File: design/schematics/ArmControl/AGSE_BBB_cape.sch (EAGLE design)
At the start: 57 parts, among them Q1 PFET-FQP27P06, Q2 PFET-FQP27P06, Q3 NFET-FQP30N06L, Q4 NFET-FQP30N06L, Q5 PFET-FQP27P06, Q6 PFET-FQP27P06, Q7 NFET-FQP30N06L, Q8 NFET-FQP30N06L, U1 V_REG_LD1085D2

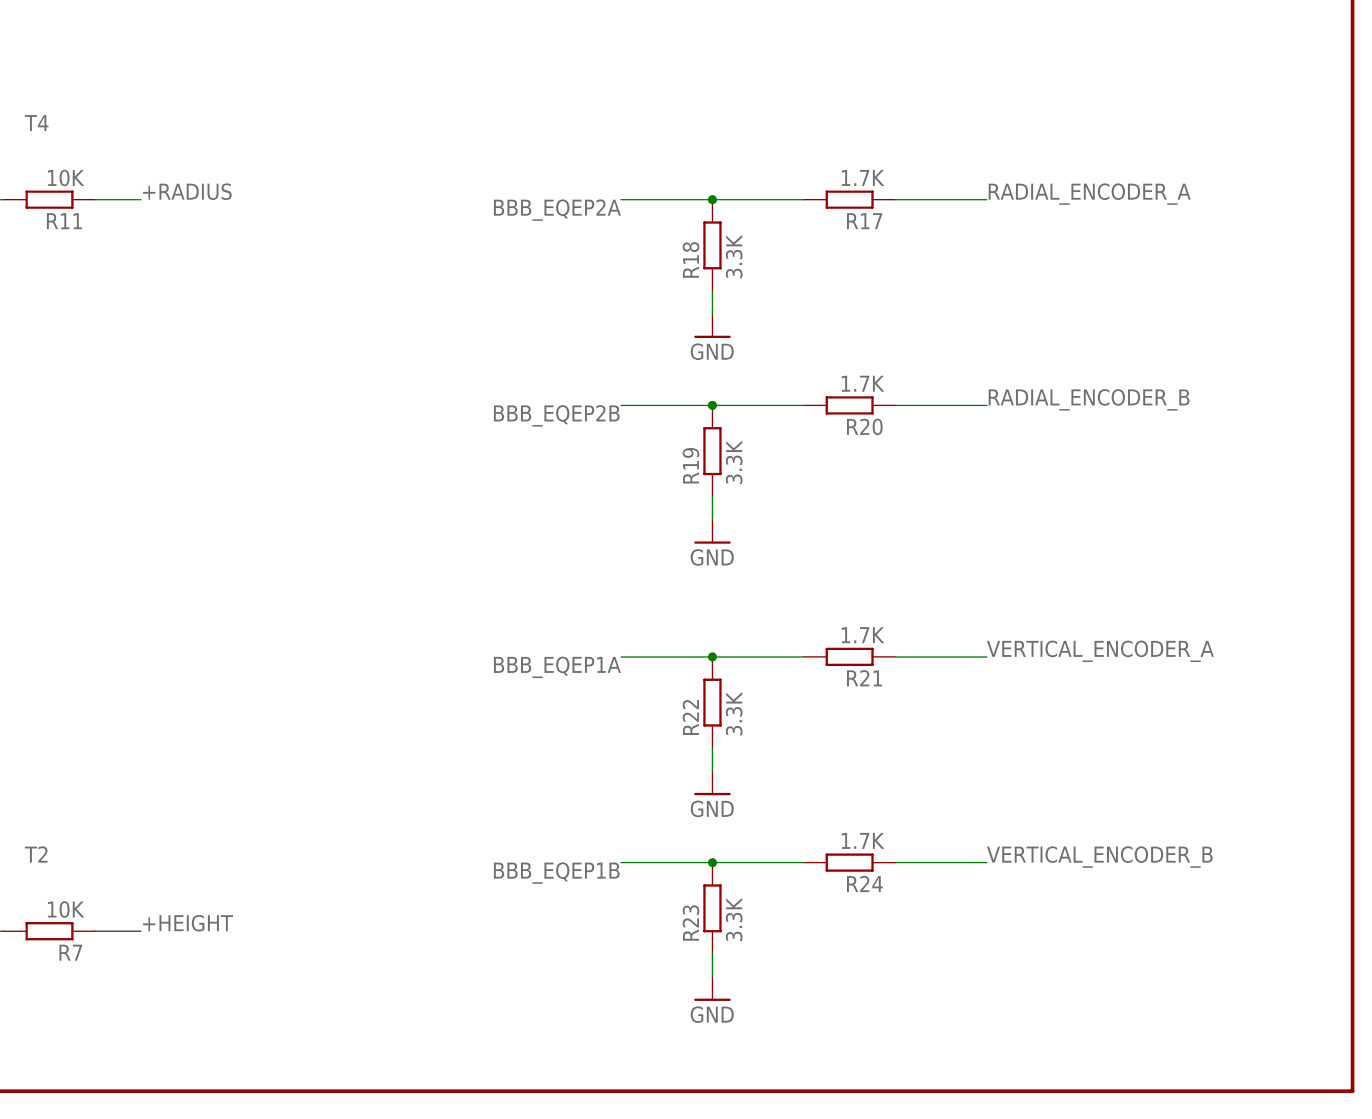
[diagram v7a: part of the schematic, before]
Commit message: Updated board to have molex 4-pin encoder connectors
* also removed unneeded zips
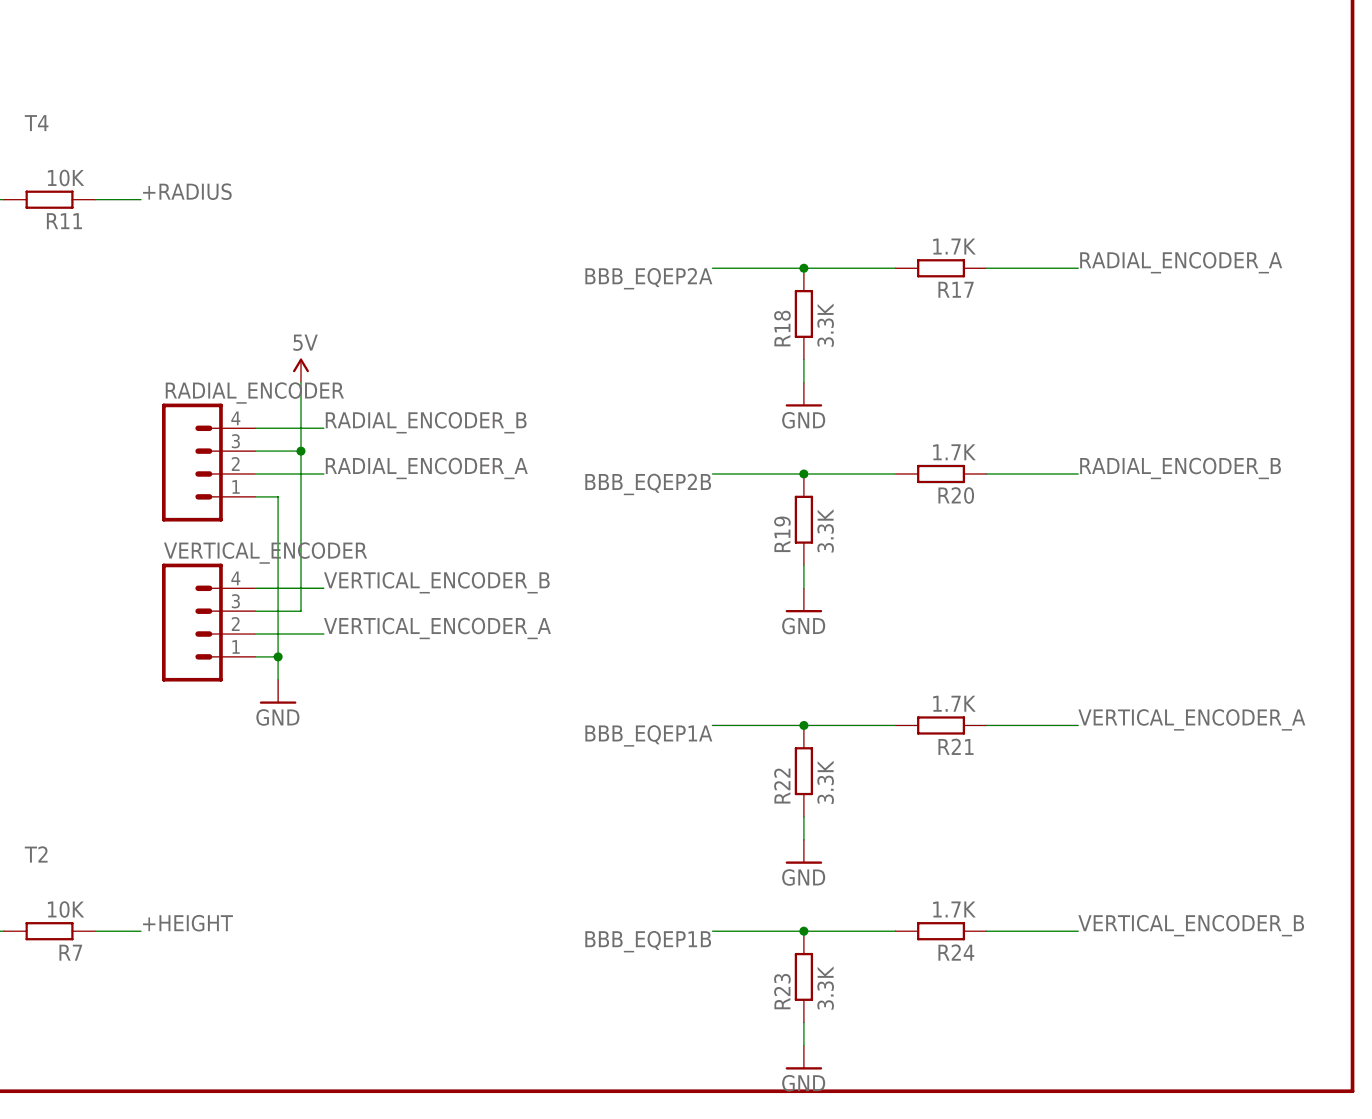
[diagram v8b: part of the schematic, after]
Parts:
- added RADIAL_ENCODER, VERTICAL_ENCODER: (no value), SparkFun-Connectors:M04POLAR
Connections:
- net 5V: now also RADIAL_ENCODER.3, VERTICAL_ENCODER.3
- net GND: now also RADIAL_ENCODER.1, VERTICAL_ENCODER.1
- net RADIAL_ENCODER_A: now also RADIAL_ENCODER.2
- net RADIAL_ENCODER_B: now also RADIAL_ENCODER.4
- net VERTICAL_ENCODER_A: now also VERTICAL_ENCODER.2
- net VERTICAL_ENCODER_B: now also VERTICAL_ENCODER.4
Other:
- moved on the sheet: R17, R18, R19, R20, R21, R22, R23, R24
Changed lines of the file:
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@@
 <part name="R26" library="resistor" deviceset="R-EU_" device="M0805" value="50"/>
 <part name="R27" library="resistor" deviceset="R-EU_" device="M0805" value="50"/>
+<part name="RADIAL_ENCODER" library="SparkFun-Connectors" deviceset="M04" device="POLAR"/>
+<part name="VERTICAL_ENCODER" library="SparkFun-Connectors" deviceset="M04" device="POLAR"/>
+<part name="GND8" library="supply1" deviceset="GND" device=""/>
+<part name="SUPPLY4" library="SparkFun-Aesthetics" deviceset="5V" device=""/>
 </parts>
 <sheets>
@@
 <instance part="R16" gate="G$1" x="208.28" y="121.92" rot="R90"/>
 <instance part="GND12" gate="1" x="208.28" y="111.76"/>
-<instance part="R17" gate="G$1" x="312.42" y="30.48" rot="R180"/>
-<instance part="R18" gate="G$1" x="297.18" y="25.4" rot="R90"/>
-<instance part="R19" gate="G$1" x="297.18" y="2.54" rot="R90"/>
-<instance part="R20" gate="G$1" x="312.42" y="7.62" rot="R180"/>
-<instance part="GND13" gate="1" x="297.18" y="-7.62"/>
-<instance part="GND14" gate="1" x="297.18" y="15.24"/>
-<instance part="R21" gate="G$1" x="312.42" y="-20.32" rot="R180"/>
-<instance part="R22" gate="G$1" x="297.18" y="-25.4" rot="R90"/>
-<instance part="R23" gate="G$1" x="297.18" y="-48.26" rot="R90"/>
-<instance part="R24" gate="G$1" x="312.42" y="-43.18" rot="R180"/>
-<instance part="GND15" gate="1" x="297.18" y="-58.42"/>
-<instance part="GND16" gate="1" x="297.18" y="-35.56"/>
+<instance part="R17" gate="G$1" x="322.58" y="22.86" rot="R180"/>
+<instance part="R18" gate="G$1" x="307.34" y="17.78" rot="R90"/>
+<instance part="R19" gate="G$1" x="307.34" y="-5.08" rot="R90"/>
+<instance part="R20" gate="G$1" x="322.58" y="0" rot="R180"/>
+<instance part="GND13" gate="1" x="307.34" y="-15.24"/>
+<instance part="GND14" gate="1" x="307.34" y="7.62"/>
+<instance part="R21" gate="G$1" x="322.58" y="-27.94" rot="R180"/>
+<instance part="R22" gate="G$1" x="307.34" y="-33.02" rot="R90"/>
+<instance part="R23" gate="G$1" x="307.34" y="-55.88" rot="R90"/>
+<instance part="R24" gate="G$1" x="322.58" y="-50.8" rot="R180"/>
+<instance part="GND15" gate="1" x="307.34" y="-66.04"/>
+<instance part="GND16" gate="1" x="307.34" y="-43.18"/>
 <instance part="FRAME1" gate="G$1" x="-63.5" y="-68.58"/>
 <instance part="FRAME1" gate="G$2" x="-63.5" y="-68.58"/>
@@
 <instance part="R26" gate="G$1" x="91.44" y="-20.32" rot="R90"/>
 <instance part="R27" gate="G$1" x="83.82" y="-20.32" rot="R90"/>
+<instance part="RADIAL_ENCODER" gate="G$1" x="241.3" y="0"/>
+<instance part="VERTICAL_ENCODER" gate="G$1" x="241.3" y="-17.78"/>
+<instance part="GND8" gate="1" x="248.92" y="-25.4"/>
+<instance part="SUPPLY4" gate="G$1" x="251.46" y="10.16"/>
 </instances>
 <busses>
@@
 <pinref part="R19" gate="G$1" pin="1"/>
 <pinref part="GND13" gate="1" pin="GND"/>
-<wire x1="297.18" y1="-5.08" x2="297.18" y2="-2.54" width="0.1524" layer="91"/>
+<wire x1="307.34" y1="-12.7" x2="307.34" y2="-10.16" width="0.1524" layer="91"/>
 </segment>
 <segment>
 <pinref part="R18" gate="G$1" pin="1"/>
 <pinref part="GND14" gate="1" pin="GND"/>
-<wire x1="297.18" y1="17.78" x2="297.18" y2="20.32" width="0.1524" layer="91"/>
+<wire x1="307.34" y1="10.16" x2="307.34" y2="12.7" width="0.1524" layer="91"/>
 </segment>
 <segment>
 <pinref part="R23" gate="G$1" pin="1"/>
 <pinref part="GND15" gate="1" pin="GND"/>
-<wire x1="297.18" y1="-55.88" x2="297.18" y2="-53.34" width="0.1524" layer="91"/>
+<wire x1="307.34" y1="-63.5" x2="307.34" y2="-60.96" width="0.1524" layer="91"/>
 </segment>
 <segment>
 <pinref part="R22" gate="G$1" pin="1"/>
 <pinref part="GND16" gate="1" pin="GND"/>
-<wire x1="297.18" y1="-33.02" x2="297.18" y2="-30.48" width="0.1524" layer="91"/>
+<wire x1="307.34" y1="-40.64" x2="307.34" y2="-38.1" width="0.1524" layer="91"/>
 </segment>
 <segment>
@@
 <junction x="106.68" y="-27.94"/>
 </segment>
+<segment>
+<pinref part="RADIAL_ENCODER" gate="G$1" pin="1"/>
+<wire x1="246.38" y1="-2.54" x2="248.92" y2="-2.54" width="0.1524" layer="91"/>
+<wire x1="248.92" y1="-2.54" x2="248.92" y2="-20.32" width="0.1524" layer="91"/>
+<pinref part="VERTICAL_ENCODER" gate="G$1" pin="1"/>
+<wire x1="248.92" y1="-20.32" x2="248.92" y2="-22.86" width="0.1524" layer="91"/>
+<wire x1="246.38" y1="-20.32" x2="248.92" y2="-20.32" width="0.1524" layer="91"/>
+<junction x="248.92" y="-20.32"/>
+<pinref part="GND8" gate="1" pin="GND"/>
+</segment>
 </net>
 <net name="N$3" class="0">
@@
 <wire x1="345.44" y1="124.46" x2="345.44" y2="132.08" width="0.1524" layer="91"/>
 <pinref part="SUPPLY3" gate="G$1" pin="5V"/>
+</segment>
+<segment>
+<pinref part="VERTICAL_ENCODER" gate="G$1" pin="3"/>
+<wire x1="246.38" y1="-15.24" x2="251.46" y2="-15.24" width="0.1524" layer="91"/>
+<pinref part="SUPPLY4" gate="G$1" pin="5V"/>
+<wire x1="251.46" y1="-15.24" x2="251.46" y2="2.54" width="0.1524" layer="91"/>
+<pinref part="RADIAL_ENCODER" gate="G$1" pin="3"/>
+<wire x1="251.46" y1="2.54" x2="251.46" y2="10.16" width="0.1524" layer="91"/>
+<wire x1="246.38" y1="2.54" x2="251.46" y2="2.54" width="0.1524" layer="91"/>
+<junction x="251.46" y="2.54"/>
 </segment>
 </net>
@@
 <pinref part="R18" gate="G$1" pin="2"/>
 <pinref part="R17" gate="G$1" pin="2"/>
-<wire x1="307.34" y1="30.48" x2="297.18" y2="30.48" width="0.1524" layer="91"/>
-<junction x="297.18" y="30.48"/>
-<wire x1="297.18" y1="30.48" x2="287.02" y2="30.48" width="0.1524" layer="91"/>
-<label x="287.02" y="30.48" size="1.778" layer="95" rot="R180"/>
+<wire x1="317.5" y1="22.86" x2="307.34" y2="22.86" width="0.1524" layer="91"/>
+<junction x="307.34" y="22.86"/>
+<wire x1="307.34" y1="22.86" x2="297.18" y2="22.86" width="0.1524" layer="91"/>
+<label x="297.18" y="22.86" size="1.778" layer="95" rot="R180"/>
 </segment>
 <segment>
@@
 <pinref part="R19" gate="G$1" pin="2"/>
 <pinref part="R20" gate="G$1" pin="2"/>
-<wire x1="307.34" y1="7.62" x2="297.18" y2="7.62" width="0.1524" layer="91"/>
-<junction x="297.18" y="7.62"/>
-<wire x1="297.18" y1="7.62" x2="287.02" y2="7.62" width="0.1524" layer="91"/>
-<label x="287.02" y="7.62" size="1.778" layer="95" rot="R180"/>
+<wire x1="317.5" y1="0" x2="307.34" y2="0" width="0.1524" layer="91"/>
+<junction x="307.34" y="0"/>
+<wire x1="307.34" y1="0" x2="297.18" y2="0" width="0.1524" layer="91"/>
+<label x="297.18" y="0" size="1.778" layer="95" rot="R180"/>
 </segment>
 <segment>
@@
 <segment>
 <pinref part="R20" gate="G$1" pin="1"/>
-<wire x1="317.5" y1="7.62" x2="327.66" y2="7.62" width="0.1524" layer="91"/>
-<label x="327.66" y="7.62" size="1.778" layer="95"/>
+<wire x1="327.66" y1="0" x2="337.82" y2="0" width="0.1524" layer="91"/>
+<label x="337.82" y="0" size="1.778" layer="95"/>
+</segment>
+<segment>
+<pinref part="RADIAL_ENCODER" gate="G$1" pin="4"/>
+<wire x1="246.38" y1="5.08" x2="254" y2="5.08" width="0.1524" layer="91"/>
+<label x="254" y="5.08" size="1.778" layer="95"/>
 </segment>
 </net>
@@
 <segment>
 <pinref part="R17" gate="G$1" pin="1"/>
-<wire x1="317.5" y1="30.48" x2="327.66" y2="30.48" width="0.1524" layer="91"/>
-<label x="327.66" y="30.48" size="1.778" layer="95"/>
+<wire x1="327.66" y1="22.86" x2="337.82" y2="22.86" width="0.1524" layer="91"/>
+<label x="337.82" y="22.86" size="1.778" layer="95"/>
+</segment>
+<segment>
+<pinref part="RADIAL_ENCODER" gate="G$1" pin="2"/>
+<wire x1="246.38" y1="0" x2="254" y2="0" width="0.1524" layer="91"/>
+<label x="254" y="0" size="1.778" layer="95"/>
 </segment>
 </net>
@@
 <pinref part="R22" gate="G$1" pin="2"/>
 <pinref part="R21" gate="G$1" pin="2"/>
-<wire x1="307.34" y1="-20.32" x2="297.18" y2="-20.32" width="0.1524" layer="91"/>
-<junction x="297.18" y="-20.32"/>
-<wire x1="297.18" y1="-20.32" x2="287.02" y2="-20.32" width="0.1524" layer="91"/>
-<label x="287.02" y="-20.32" size="1.778" layer="95" rot="R180"/>
+<wire x1="317.5" y1="-27.94" x2="307.34" y2="-27.94" width="0.1524" layer="91"/>
+<junction x="307.34" y="-27.94"/>
+<wire x1="307.34" y1="-27.94" x2="297.18" y2="-27.94" width="0.1524" layer="91"/>
+<label x="297.18" y="-27.94" size="1.778" layer="95" rot="R180"/>
 </segment>
 <segment>
@@
 <pinref part="R23" gate="G$1" pin="2"/>
 <pinref part="R24" gate="G$1" pin="2"/>
-<wire x1="307.34" y1="-43.18" x2="297.18" y2="-43.18" width="0.1524" layer="91"/>
-<junction x="297.18" y="-43.18"/>
-<wire x1="297.18" y1="-43.18" x2="287.02" y2="-43.18" width="0.1524" layer="91"/>
-<label x="287.02" y="-43.18" size="1.778" layer="95" rot="R180"/>
+<wire x1="317.5" y1="-50.8" x2="307.34" y2="-50.8" width="0.1524" layer="91"/>
+<junction x="307.34" y="-50.8"/>
+<wire x1="307.34" y1="-50.8" x2="297.18" y2="-50.8" width="0.1524" layer="91"/>
+<label x="297.18" y="-50.8" size="1.778" layer="95" rot="R180"/>
 </segment>
 <segment>
@@
 <segment>
 <pinref part="R24" gate="G$1" pin="1"/>
-<wire x1="317.5" y1="-43.18" x2="327.66" y2="-43.18" width="0.1524" layer="91"/>
-<label x="327.66" y="-43.18" size="1.778" layer="95"/>
+<wire x1="327.66" y1="-50.8" x2="337.82" y2="-50.8" width="0.1524" layer="91"/>
+<label x="337.82" y="-50.8" size="1.778" layer="95"/>
+</segment>
+<segment>
+<pinref part="VERTICAL_ENCODER" gate="G$1" pin="4"/>
+<wire x1="246.38" y1="-12.7" x2="254" y2="-12.7" width="0.1524" layer="91"/>
+<label x="254" y="-12.7" size="1.778" layer="95"/>
 </segment>
 </net>
@@
 <segment>
 <pinref part="R21" gate="G$1" pin="1"/>
-<wire x1="317.5" y1="-20.32" x2="327.66" y2="-20.32" width="0.1524" layer="91"/>
-<label x="327.66" y="-20.32" size="1.778" layer="95"/>
-</segment>
-</net>
+<wire x1="327.66" y1="-27.94" x2="337.82" y2="-27.94" width="0.1524" layer="91"/>
+<label x="337.82" y="-27.94" size="1.778" layer="95"/>
+</segment>
+<segment>
+<pinref part="VERTICAL_ENCODER" gate="G$1" pin="2"/>
+<wire x1="246.38" y1="-17.78" x2="254" y2="-17.78" width="0.1524" layer="91"/>
+<label x="254" y="-17.78" size="1.778" layer="95"/>
+</segment>
+</net>
